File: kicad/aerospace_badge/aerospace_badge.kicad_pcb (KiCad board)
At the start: 2 copper layers, 134.3 x 140 mm, 19 parts, among them J1 Conn_02x03_Counter_Clockwise, J2 Conn_01x02, J3 Conn_01x01_Male, J4 Conn_01x02, J5 Conn_01x03, J6 Conn_01x01_Male, J7 Conn_01x01_Male, U1 ATtiny85-20SU

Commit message: updated footprints per new datasheets.
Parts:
- D1: footprint sunled:XZDGK45WT-9 -> sunled:XZMYK45WT-9
- D3: footprint sunled:XZDGK45WT-9 -> sunled:XZM2CRK45WT-9
- J5: value Conn_01x03 -> Conn_01x04; footprint Connector_PinHeader_2.54mm:PinHeader_1x03_P2.54mm_Vertical -> Connector_PinHeader_2.54mm:PinHeader_1x04_P2.54mm_Vertical; moved to F.Cu
- moved J5 13.5 mm to (136.7, 110.6), turned to 180 degrees
- moved D2 0.05 mm to (210.6, 115.5)
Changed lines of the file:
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@@
     (add_net VCC)
+  )
+  (module sunled:XZMYK45WT-9 (layer B.Cu)
+    (at 148.2379 26.1747 180)
+    (fp_text reference D1 (at 5.10286 0.32512 90) (layer B.SilkS)
+      (effects (font (size 1 1) (thickness 0.15)) (justify mirror))
+    )
+    (fp_text value LED (at 0.66802 2.89052) (layer F.Fab) hide
+      (effects (font (size 1 1) (thickness 0.15)))
+    )
+    (fp_circle (center -0.01524 -0.14214) (end 0.78476 -0.14214) (layer B.Mask) (width 1.6))
+    (fp_circle (center -3.69824 -1.5621) (end -3.49824 -1.5621) (layer B.SilkS) (width 0.4))
+    (pad 1 smd rect (at -2.6 0 180) (size 1.4 2.6) (layers B.Cu B.Paste B.Mask)
+      (net 1 GND))
+    (pad 2 smd rect (at 2.6 0 180) (size 1.4 2.6) (layers B.Cu B.Paste B.Mask)
+      (net 3 "Net-(D1-Pad2)"))
+  )
+  (module sunled:XZM2CRK45WT-9 (layer B.Cu)
+    (at 86.178395 115.666201 35)
+    (fp_text reference D3 (at 5.10286 0.325119 -235) (layer B.SilkS)
+      (effects (font (size 1 1) (thickness 0.15)) (justify mirror))
+    )
+    (fp_text value LED (at 0.66802 2.89052 35) (layer F.Fab) hide
+      (effects (font (size 1 1) (thickness 0.15)))
+    )
+    (fp_circle (center 3.64744 1.44018) (end 3.84744 1.44018) (layer B.SilkS) (width 0.4))
+    (fp_circle (center -0.01524 -0.14214) (end 0.78476 -0.14214) (layer B.Mask) (width 1.6))
+    (pad 1 smd rect (at -2.6 0 35) (size 1.4 2.6) (layers B.Cu B.Paste B.Mask)
+      (net 1 GND))
+    (pad 2 smd rect (at 2.6 0 35) (size 1.4 2.6) (layers B.Cu B.Paste B.Mask)
+      (net 5 "Net-(D3-Pad2)"))
+  )
+  (module sunled:XZDGK45WT-9 (layer B.Cu)
+    (at 210.601916 115.475948 140)
+    (fp_text reference D2 (at 4.21386 0.0889 50) (layer B.SilkS)
+      (effects (font (size 1 1) (thickness 0.15)) (justify mirror))
+    )
+    (fp_text value LED (at -0.11176 2.13106 320) (layer F.Fab) hide
+      (effects (font (size 1 1) (thickness 0.15)))
+    )
+    (fp_circle (center -3.69824 -1.5621) (end -3.49824 -1.5621) (layer B.SilkS) (width 0.4))
+    (fp_circle (center -0.01524 -0.14214) (end 0.78476 -0.14214) (layer B.Mask) (width 1.6))
+    (pad 2 smd rect (at 2.6 0 140) (size 1.4 2.6) (layers B.Cu B.Paste B.Mask)
+      (net 4 "Net-(D2-Pad2)"))
+    (pad 1 smd rect (at -2.6 0 140) (size 1.4 2.6) (layers B.Cu B.Paste B.Mask)
+      (net 1 GND))
   )
   (module aerospace_badge:isp_pad (layer B.Cu)
@@
       (net 12 "Net-(J2-Pad1)"))
   )
-  (module sunled:XZDGK45WT-9 (layer B.Cu)
-    (at 210.613034 115.5273 140)
-    (fp_text reference D2 (at 4.21386 0.0889 50) (layer B.SilkS)
-      (effects (font (size 1 1) (thickness 0.15)) (justify mirror))
-    )
-    (fp_text value LED (at -0.11176 2.13106 320) (layer F.Fab) hide
-      (effects (font (size 1 1) (thickness 0.15)))
-    )
-    (fp_circle (center -0.01524 -0.14214) (end 0.78476 -0.14214) (layer B.Mask) (width 1.6))
-    (fp_circle (center 3.66268 -1.63068) (end 3.86268 -1.63068) (layer B.SilkS) (width 0.4))
-    (pad 2 smd rect (at 2.6 0 140) (size 1.4 2.6) (layers B.Cu B.Paste B.Mask)
-      (net 4 "Net-(D2-Pad2)"))
-    (pad 1 smd rect (at -2.6 0 140) (size 1.4 2.6) (layers B.Cu B.Paste B.Mask)
-      (net 1 GND))
-  )
-  (module sunled:XZDGK45WT-9 (layer B.Cu)
-    (at 86.203795 115.678901 35)
-    (fp_text reference D3 (at 4.63042 0.127 -55) (layer B.SilkS)
-      (effects (font (size 1 1) (thickness 0.15)) (justify mirror))
-    )
-    (fp_text value LED (at -0.11176 2.13106 35) (layer F.Fab) hide
-      (effects (font (size 1 1) (thickness 0.15)))
-    )
-    (fp_circle (center -0.01524 -0.14214) (end 0.78476 -0.14214) (layer B.Mask) (width 1.6))
-    (fp_circle (center 3.66268 -1.63068) (end 3.86268 -1.63068) (layer B.SilkS) (width 0.4))
-    (pad 2 smd rect (at 2.6 0 35) (size 1.4 2.6) (layers B.Cu B.Paste B.Mask)
-      (net 5 "Net-(D3-Pad2)"))
-    (pad 1 smd rect (at -2.6 0 35) (size 1.4 2.6) (layers B.Cu B.Paste B.Mask)
-      (net 1 GND))
-  )
-  (module sunled:XZDGK45WT-9 (layer B.Cu)
-    (at 148.2471 26.1747 180)
-    (fp_text reference D1 (at 0.2159 -2.6162) (layer B.SilkS)
-      (effects (font (size 1 1) (thickness 0.15)) (justify mirror))
-    )
-    (fp_text value LED (at -0.11176 2.13106) (layer F.Fab) hide
-      (effects (font (size 1 1) (thickness 0.15)))
-    )
-    (fp_circle (center -0.01524 -0.14214) (end 0.78476 -0.14214) (layer B.Mask) (width 1.6))
-    (fp_circle (center 3.66268 -1.63068) (end 3.86268 -1.63068) (layer B.SilkS) (width 0.4))
-    (pad 2 smd rect (at 2.6 0 180) (size 1.4 2.6) (layers B.Cu B.Paste B.Mask)
-      (net 3 "Net-(D1-Pad2)"))
-    (pad 1 smd rect (at -2.6 0 180) (size 1.4 2.6) (layers B.Cu B.Paste B.Mask)
-      (net 1 GND))
-  )
   (module aerospace_badge:linx_sma_jack_female_socket (layer B.Cu)
     (at 169.8371 75.661 180)
@@
     )
   )
-  (module Connector_PinHeader_2.54mm:PinHeader_1x03_P2.54mm_Vertical (layer B.Cu)
-    (at 138.2522 97.2058 90)
-    (descr "Through hole straight pin header, 1x03, 2.54mm pitch, single row")
-    (tags "Through hole pin header THT 1x03 2.54mm single row")
-    (fp_text reference J5 (at 0 2.33 -90) (layer B.SilkS)
-      (effects (font (size 1 1) (thickness 0.15)) (justify mirror))
-    )
-    (fp_text value Conn_01x03 (at 0 -7.41 -90) (layer B.Fab)
-      (effects (font (size 1 1) (thickness 0.15)) (justify mirror))
-    )
-    (fp_line (start 1.8 1.8) (end -1.8 1.8) (layer B.CrtYd) (width 0.05))
-    (fp_line (start 1.8 -6.85) (end 1.8 1.8) (layer B.CrtYd) (width 0.05))
-    (fp_line (start -1.8 -6.85) (end 1.8 -6.85) (layer B.CrtYd) (width 0.05))
-    (fp_line (start -1.8 1.8) (end -1.8 -6.85) (layer B.CrtYd) (width 0.05))
-    (fp_line (start -1.33 1.33) (end 0 1.33) (layer B.SilkS) (width 0.12))
-    (fp_line (start -1.33 0) (end -1.33 1.33) (layer B.SilkS) (width 0.12))
-    (fp_line (start -1.33 -1.27) (end 1.33 -1.27) (layer B.SilkS) (width 0.12))
-    (fp_line (start 1.33 -1.27) (end 1.33 -6.41) (layer B.SilkS) (width 0.12))
-    (fp_line (start -1.33 -1.27) (end -1.33 -6.41) (layer B.SilkS) (width 0.12))
-    (fp_line (start -1.33 -6.41) (end 1.33 -6.41) (layer B.SilkS) (width 0.12))
-    (fp_line (start -1.27 0.635) (end -0.635 1.27) (layer B.Fab) (width 0.1))
-    (fp_line (start -1.27 -6.35) (end -1.27 0.635) (layer B.Fab) (width 0.1))
-    (fp_line (start 1.27 -6.35) (end -1.27 -6.35) (layer B.Fab) (width 0.1))
-    (fp_line (start 1.27 1.27) (end 1.27 -6.35) (layer B.Fab) (width 0.1))
-    (fp_line (start -0.635 1.27) (end 1.27 1.27) (layer B.Fab) (width 0.1))
-    (fp_text user %R (at 0 -2.54) (layer B.Fab)
-      (effects (font (size 1 1) (thickness 0.15)) (justify mirror))
-    )
-    (pad 1 thru_hole rect (at 0 0 90) (size 1.7 1.7) (drill 1) (layers *.Cu *.Mask)
-      (net 9 "Net-(J1-Pad3)"))
-    (pad 2 thru_hole oval (at 0 -2.54 90) (size 1.7 1.7) (drill 1) (layers *.Cu *.Mask)
-      (net 10 "Net-(J1-Pad4)"))
-    (pad 3 thru_hole oval (at 0 -5.08 90) (size 1.7 1.7) (drill 1) (layers *.Cu *.Mask)
-      (net 1 GND))
-  )
   (module aerospace_badge:led_in-s124ar (layer B.Cu)
     (at 143.3957 119.6319 90)
@@
       (net 15 "Net-(J4-Pad1)"))
   )
+  (module Connector_PinHeader_2.54mm:PinHeader_1x04_P2.54mm_Vertical (layer F.Cu)
+    (at 136.6647 110.5662 180)
+    (descr "Through hole straight pin header, 1x04, 2.54mm pitch, single row")
+    (tags "Through hole pin header THT 1x04 2.54mm single row")
+    (fp_text reference J5 (at 0 -2.33) (layer F.SilkS)
+      (effects (font (size 1 1) (thickness 0.15)))
+    )
+    (fp_text value Conn_01x04 (at 0 9.95) (layer F.Fab)
+      (effects (font (size 1 1) (thickness 0.15)))
+    )
+    (fp_line (start -0.635 -1.27) (end 1.27 -1.27) (layer F.Fab) (width 0.1))
+    (fp_line (start 1.27 -1.27) (end 1.27 8.89) (layer F.Fab) (width 0.1))
+    (fp_line (start 1.27 8.89) (end -1.27 8.89) (layer F.Fab) (width 0.1))
+    (fp_line (start -1.27 8.89) (end -1.27 -0.635) (layer F.Fab) (width 0.1))
+    (fp_line (start -1.27 -0.635) (end -0.635 -1.27) (layer F.Fab) (width 0.1))
+    (fp_line (start -1.33 8.95) (end 1.33 8.95) (layer F.SilkS) (width 0.12))
+    (fp_line (start -1.33 1.27) (end -1.33 8.95) (layer F.SilkS) (width 0.12))
+    (fp_line (start 1.33 1.27) (end 1.33 8.95) (layer F.SilkS) (width 0.12))
+    (fp_line (start -1.33 1.27) (end 1.33 1.27) (layer F.SilkS) (width 0.12))
+    (fp_line (start -1.33 0) (end -1.33 -1.33) (layer F.SilkS) (width 0.12))
+    (fp_line (start -1.33 -1.33) (end 0 -1.33) (layer F.SilkS) (width 0.12))
+    (fp_line (start -1.8 -1.8) (end -1.8 9.4) (layer F.CrtYd) (width 0.05))
+    (fp_line (start -1.8 9.4) (end 1.8 9.4) (layer F.CrtYd) (width 0.05))
+    (fp_line (start 1.8 9.4) (end 1.8 -1.8) (layer F.CrtYd) (width 0.05))
+    (fp_line (start 1.8 -1.8) (end -1.8 -1.8) (layer F.CrtYd) (width 0.05))
+    (fp_text user %R (at 0 3.81 90) (layer F.Fab)
+      (effects (font (size 1 1) (thickness 0.15)))
+    )
+    (pad 1 thru_hole rect (at 0 0 180) (size 1.7 1.7) (drill 1) (layers *.Cu *.Mask)
+      (net 9 "Net-(J1-Pad3)"))
+    (pad 2 thru_hole oval (at 0 2.54 180) (size 1.7 1.7) (drill 1) (layers *.Cu *.Mask)
+      (net 10 "Net-(J1-Pad4)"))
+    (pad 3 thru_hole oval (at 0 5.08 180) (size 1.7 1.7) (drill 1) (layers *.Cu *.Mask)
+      (net 1 GND))
+    (pad 4 thru_hole oval (at 0 7.62 180) (size 1.7 1.7) (drill 1) (layers *.Cu *.Mask)
+      (net 2 VCC))
+    (model ${KISYS3DMOD}/Connector_PinHeader_2.54mm.3dshapes/PinHeader_1x04_P2.54mm_Vertical.wrl
+      (at (xyz 0 0 0))
+      (scale (xyz 1 1 1))
+      (rotate (xyz 0 0 0))
+    )
+  )
   (gr_text "ACARS 131.550MHz\n1.779' / each wire" (at 127.4826 80.2894) (layer B.SilkS)

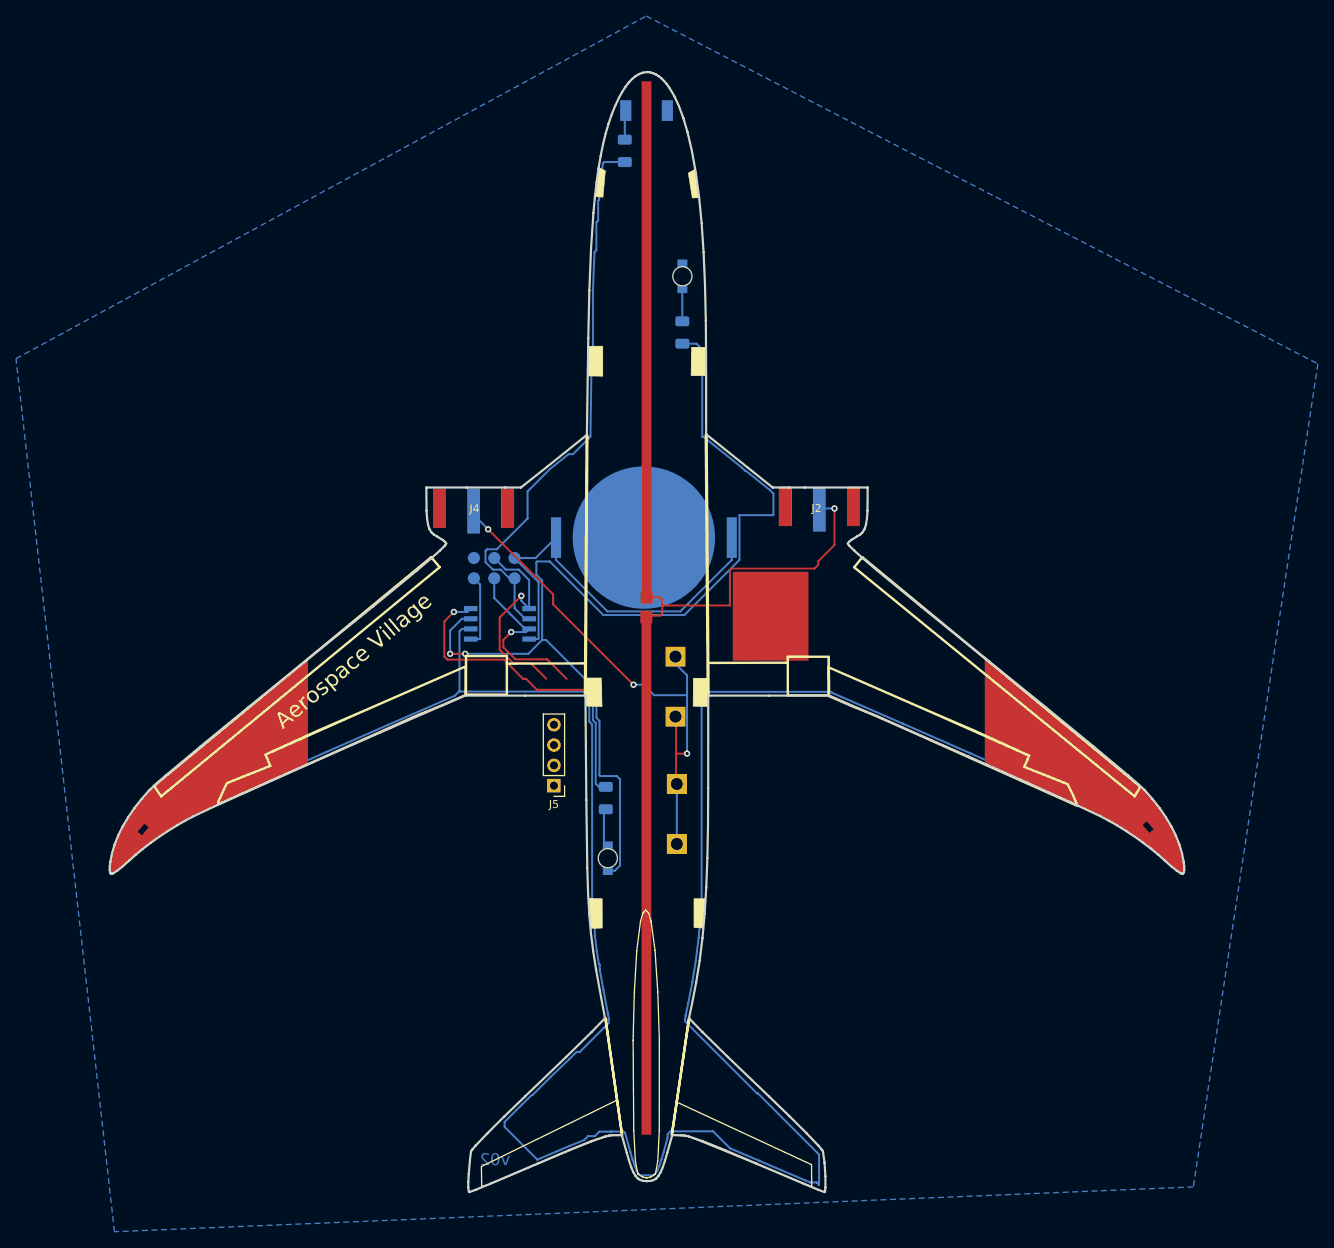
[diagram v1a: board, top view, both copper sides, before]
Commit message: updated, needs another check prior to fabrication.
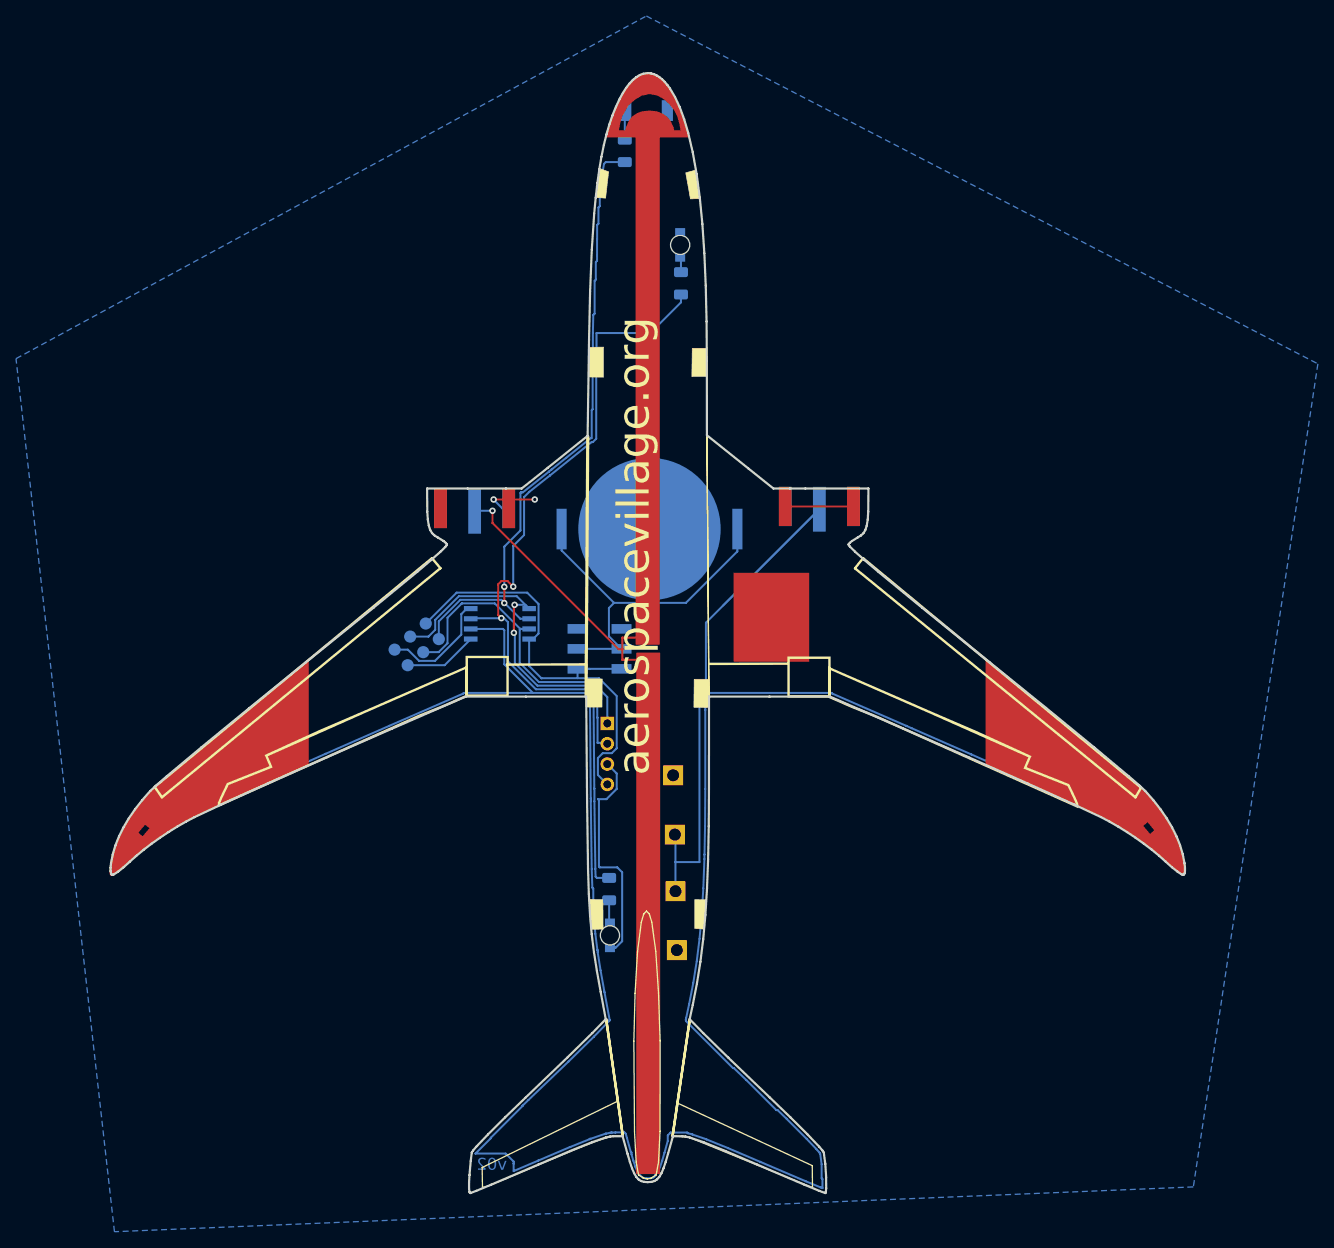
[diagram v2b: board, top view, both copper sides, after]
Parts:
- removed the J4 at (126.6, 75.9)
- added J8: Conn_01x01_Male, aerospace_badge:badge_v02, F.Cu at (148.3, 91.5)
- added SW1: SW_SPDT, aerospace_badge:switch_JS202011SCQN, B.Cu at (142.4, 93.5)
- J1: value Conn_02x03_Counter_Clockwise -> Conn_01x02; footprint aerospace_badge:isp_pad -> aerospace_badge:linx_sma_jack_female_socket
- J3: value Conn_01x01_Male -> Conn_02x03_Counter_Clockwise; footprint aerospace_badge:badge -> aerospace_badge:isp_pad; moved to B.Cu
- J4: renamed from J5; moved to B.Cu
- moved J3 28.8 mm to (119.5, 92.9), turned to 130 degrees
- moved J7 14.8 mm to (151.6, 116.8)
- moved R4 11.4 mm to (143.6, 123.5)
- moved J4 10.3 mm to (143.3, 102.8)
- moved D4 9.65 mm to (143.7, 129.3)
- moved J1 7.85 mm to (126.7, 75.9), turned to 180 degrees
- moved R5 6.15 mm to (152.5, 47.8)
- moved J6 5.77 mm to (152.0, 123.6), turned to 270 degrees
- moved D5 3.93 mm to (152.4, 43.0)
- moved BT1 1.28 mm to (148.6, 78.5)
- moved D2 0.13 mm to (210.7, 115.5)
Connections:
- BT1 pad 1: VCC -> Net-(BT1-Pad1)
- J1 pad 2: VCC -> GND
- J3 pad 1: Net-(J2-Pad1) -> Net-(J3-Pad1)
- J4 pad 1: Net-(J1-Pad3) -> Net-(J3-Pad3)
- J4 pad 2: Net-(J1-Pad4) -> Net-(J3-Pad4)
- J6 pad 1: Net-(J4-Pad1) -> Net-(J2-Pad1)
- J7 pad 1: Net-(J4-Pad1) -> Net-(J2-Pad1)
- R1 pad 1: Net-(J1-Pad1) -> Net-(J3-Pad1)
- U1 pad 1: Net-(J1-Pad5) -> Net-(J3-Pad5)
- U1 pad 5: Net-(J1-Pad4) -> Net-(J3-Pad4)
- U1 pad 6: Net-(J1-Pad1) -> Net-(J3-Pad1)
- U1 pad 7: Net-(J1-Pad3) -> Net-(J3-Pad3)
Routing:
- net Net-(J3-Pad1): track 0.00 -> 79.2 mm, vias 0 -> 2
- net Net-(J4-Pad1): track 65.3 -> 0.00 mm, vias 3 -> 0
- net Net-(J3-Pad4): track 0.00 -> 47.2 mm, vias 0 -> 2
- net Net-(BT1-Pad1): track 0.00 -> 45.0 mm
- net Net-(J3-Pad3): track 0.00 -> 40.4 mm
- net Net-(J2-Pad1): track 40.0 -> 77.5 mm, vias 1 -> 0
- net Net-(J1-Pad1): track 70.2 -> 35.7 mm, vias 0 -> 1
- net Net-(J1-Pad4): track 26.3 -> 0.00 mm, vias 1 -> 0
- net Net-(J1-Pad3): track 22.7 -> 0.00 mm, vias 1 -> 0
- net Net-(R4-Pad1): track 119.5 -> 103.7 mm
- net GND: track 89.5 -> 74.0 mm
- net Net-(R2-Pad1): track 290.1 -> 303.9 mm
- net Net-(J3-Pad5): track 0.00 -> 9.23 mm
- net Net-(J1-Pad5): track 9.05 -> 0.00 mm
- net VCC: track 51.6 -> 58.7 mm
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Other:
- board text added: "OFF"
- board text added: "ON"
- board text added: "VCC"
- board text added: "captechu.edu"
- board text removed: "Aerospace Village"
